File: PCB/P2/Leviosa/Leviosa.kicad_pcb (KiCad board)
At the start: 2 copper layers, 80 x 80 mm, 51 parts, among them J1 Barrel_Jack, J2 2.54mm 1x03 Spare

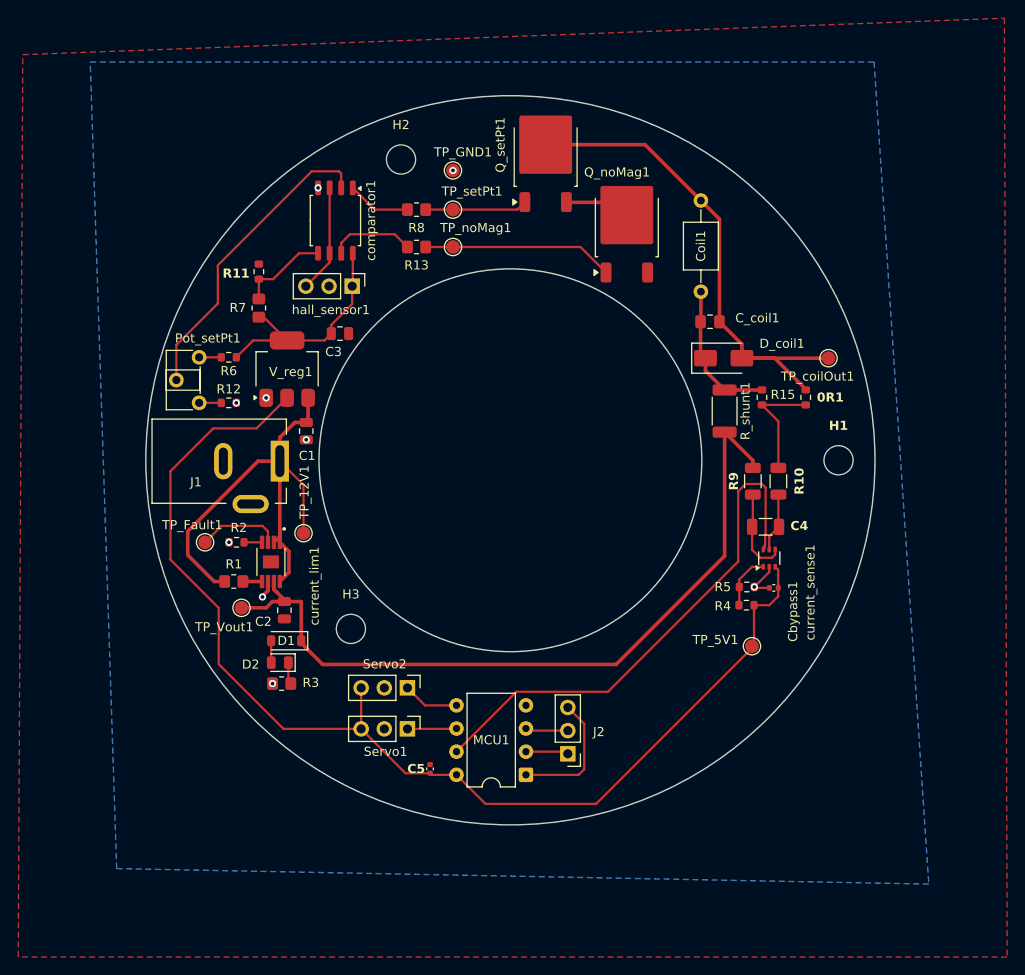
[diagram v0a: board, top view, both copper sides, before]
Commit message: update schematic and pcb per Jack's feedback
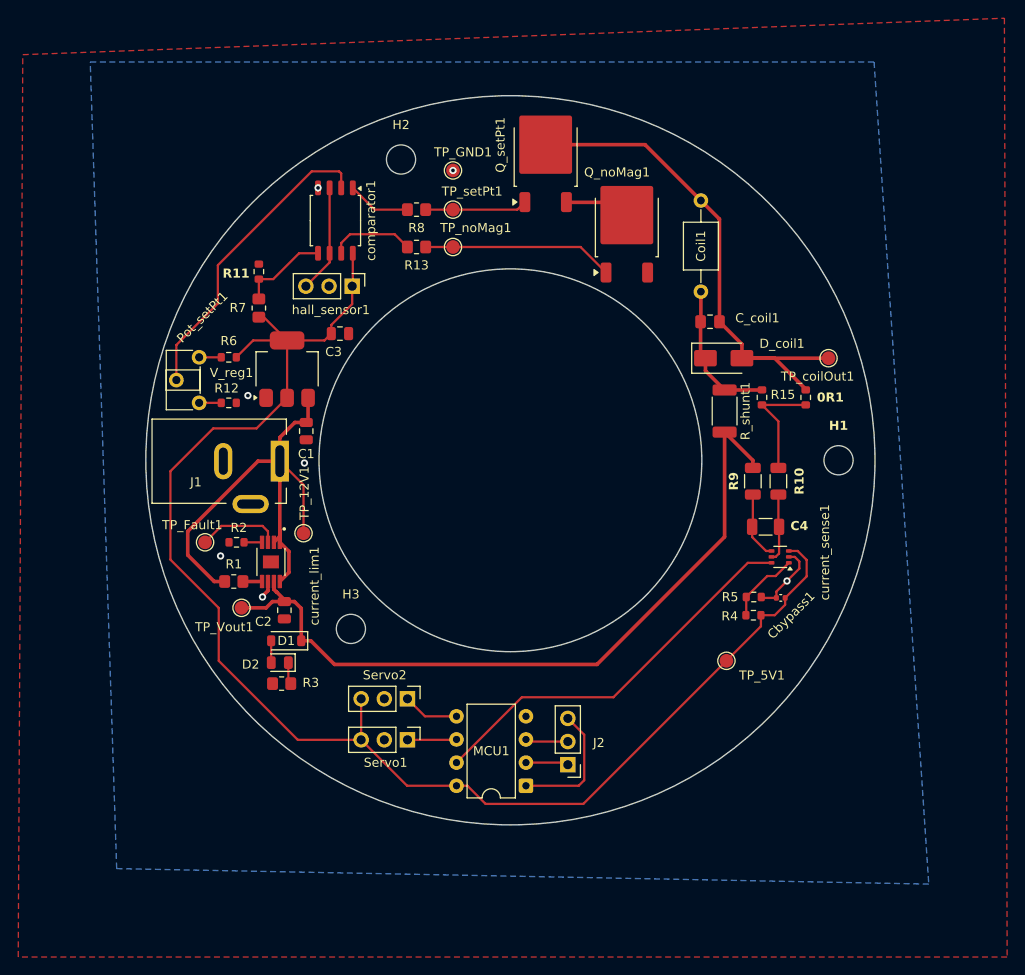
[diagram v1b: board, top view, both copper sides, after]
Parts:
- removed C5: 0.1µF, Capacitor_SMD:C_0402_1005Metric
- R10: value 8.2Ω -> 8Ω
- moved TP_5V1 3.22 mm to (123.7, 122.0)
- moved R5 1.34 mm to (126.7, 115.0)
- moved Cbypass1 1.34 mm to (129.7, 115.1)
- moved R4 1.34 mm to (126.7, 117.0)
- moved current_sense1 1.21 mm to (129.6, 110.6), turned to 180 degrees
- moved J2 1.20 mm to (106.3, 133.4)
- moved MCU1 1.20 mm to (101.7, 135.7)
- moved Servo2 1.20 mm to (88.7, 126.2)
- moved Servo1 1.20 mm to (88.7, 130.7)
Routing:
- net /current_sense: track 57.6 -> 43.6 mm
- net /5V: track 152.6 -> 162.0 mm
- net GND: track 6.54 -> 9.91 mm, vias 9 -> 7
- net Net-(current_sense1-+): track 9.69 -> 7.45 mm
- net Net-(current_sense1-REF): track 6.05 -> 8.19 mm
- net /V_out: track 85.3 -> 83.5 mm
- net Net-(current_sense1--): track 6.50 -> 7.47 mm

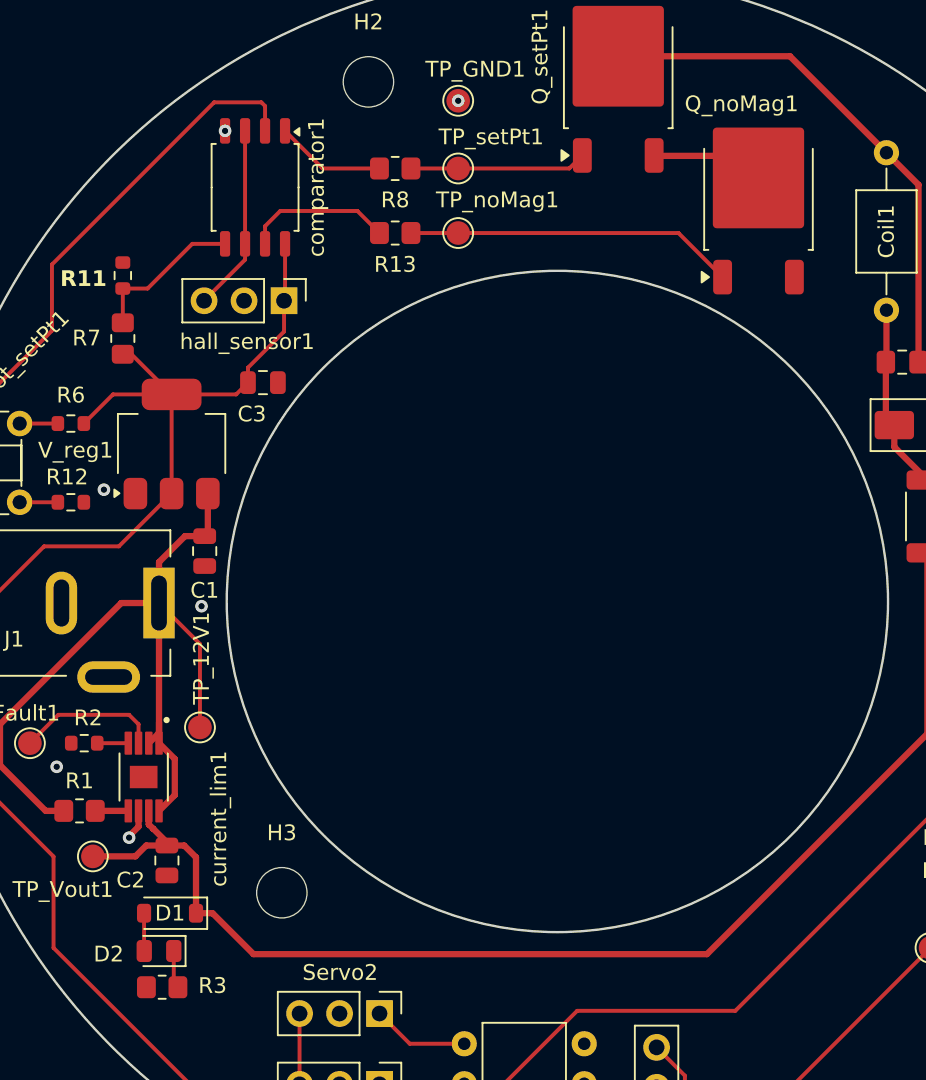
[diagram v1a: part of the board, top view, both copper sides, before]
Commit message: update PCB
pending trace width update potentially (long 5V and 12Vout)
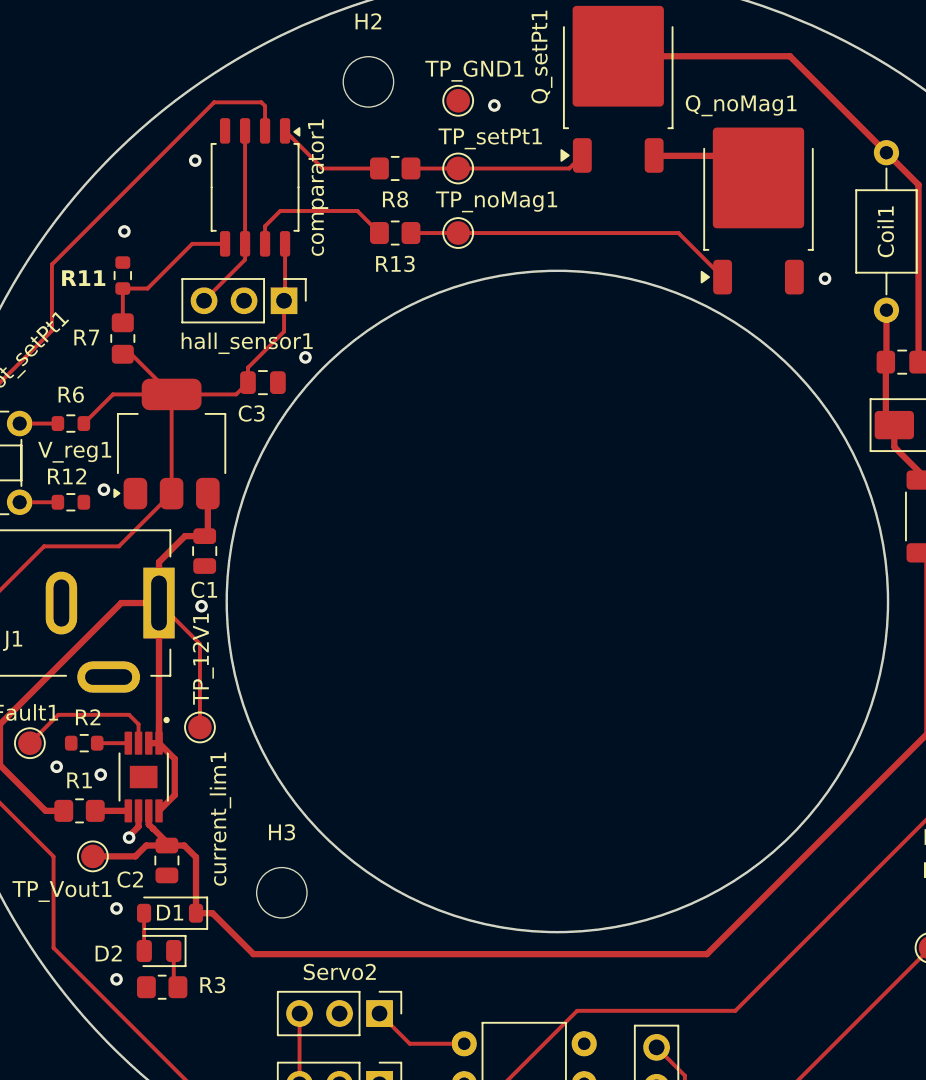
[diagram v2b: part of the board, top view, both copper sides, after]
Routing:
- net GND: vias 7 -> 13
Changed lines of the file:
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@@
+	)
+	(segment
+		(start 74.05 109)
+		(end 74.7 109)
+		(width 0.4)
+		(layer "F.Cu")
+		(net 1)
 	)
 	(segment
@@
 	)
 	(segment
-		(start 74.05 109)
-		(end 74.7 108.35)
-		(width 0.4)
-		(layer "F.Cu")
-		(net 1)
-	)
-	(segment
 		(start 77.8 93.15)
 		(end 77.8 95.65)
@@
 	)
 	(via
-		(at 78.895 70.1125)
+		(at 77 72)
+		(size 0.8)
+		(drill 0.4)
+		(layers "F.Cu" "B.Cu")
+		(net 3)
+	)
+	(via
+		(at 72.5 76.5)
 		(size 0.8)
 		(drill 0.4)
@@
 	)
 	(via
+		(at 84 84.5)
+		(size 0.8)
+		(drill 0.4)
+		(layers "F.Cu" "B.Cu")
+		(net 3)
+	)
+	(via
 		(at 130.343126 113.243126)
 		(size 0.8)
@@
 	)
 	(via
+		(at 117 79.5)
+		(size 0.8)
+		(drill 0.4)
+		(layers "F.Cu" "B.Cu")
+		(net 3)
+	)
+	(via
+		(at 72 124)
+		(size 0.8)
+		(drill 0.4)
+		(layers "F.Cu" "B.Cu")
+		(net 3)
+	)
+	(via
+		(at 72 119.5)
+		(size 0.8)
+		(drill 0.4)
+		(layers "F.Cu" "B.Cu")
+		(net 3)
+	)
+	(via
 		(at 68.2 110.5)
 		(size 0.8)
@@
 	)
 	(via
-		(at 93.7 68.2)
+		(at 96 68.5)
 		(size 0.8)
 		(drill 0.4)
@@
 		(net 3)
 	)
+	(via
+		(at 71 111)
+		(size 0.8)
+		(drill 0.4)
+		(layers "F.Cu" "B.Cu")
+		(net 3)
+	)

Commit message: update pcb
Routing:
- added copper zone on F.Cu, net +12V
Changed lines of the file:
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@@
 		(tags "LED")
 		(property "Reference" "D2"
-			(at 3.2 -0.2 0)
+			(at 3.2 0.3 0)
 			(unlocked yes)
 			(layer "F.SilkS")
@@
 	)
 	(segment
+		(start 75.5 94.15)
+		(end 73.45 96.2)
+		(width 0.8)
+		(layer "F.Cu")
+		(net 2)
+	)
+	(segment
 		(start 94.085 135.71)
 		(end 95.285 135.71)
@@
 	(segment
 		(start 75.5 93.15)
-		(end 75.5 86.85)
-		(width 0.25)
+		(end 75.5 94.15)
+		(width 0.8)
 		(layer "F.Cu")
 		(net 2)
@@
 	)
 	(segment
-		(start 72.15 96.5)
-		(end 67.4 96.5)
-		(width 0.25)
+		(start 73.45 96.2)
+		(end 67 96.2)
+		(width 0.8)
 		(layer "F.Cu")
 		(net 2)
@@
 	)
 	(segment
-		(start 76.67 130.67)
-		(end 83.625 130.67)
-		(width 0.25)
-		(layer "F.Cu")
-		(net 2)
-	)
-	(segment
 		(start 79.6 86.85)
 		(end 75.5 86.85)
@@
 	)
 	(segment
-		(start 62.7 110.9)
-		(end 68 116.2)
-		(width 0.25)
+		(start 62.9 111.2)
+		(end 68.1 116.4)
+		(width 0.8)
 		(layer "F.Cu")
 		(net 2)
@@
 	)
 	(segment
-		(start 67.4 96.5)
-		(end 62.7 101.2)
-		(width 0.25)
+		(start 77.254372 130.67)
+		(end 83.625 130.67)
+		(width 0.8)
 		(layer "F.Cu")
 		(net 2)
@@
 	)
 	(segment
-		(start 62.7 101.2)
-		(end 62.7 110.9)
+		(start 82.64 82.86)
+		(end 80.35 85.15)
 		(width 0.25)
 		(layer "F.Cu")
@@
 	)
 	(segment
-		(start 68 122)
-		(end 76.67 130.67)
-		(width 0.25)
+		(start 68.1 121.515628)
+		(end 77.254372 130.67)
+		(width 0.8)
 		(layer "F.Cu")
 		(net 2)
 	)
 	(segment
-		(start 82.64 82.86)
-		(end 80.35 85.15)
+		(start 83.625 126.17)
+		(end 83.625 130.67)
 		(width 0.25)
 		(layer "F.Cu")
@@
 	)
 	(segment
-		(start 75.5 93.15)
-		(end 72.15 96.5)
+		(start 88.665 135.71)
+		(end 83.625 130.67)
 		(width 0.25)
 		(layer "F.Cu")
@@
 	)
 	(segment
-		(start 68 116.2)
-		(end 68 122)
-		(width 0.25)
+		(start 75.5 93.15)
+		(end 75.5 86.85)
+		(width 0.8)
 		(layer "F.Cu")
 		(net 2)
 	)
 	(segment
-		(start 83.625 126.17)
-		(end 83.625 130.67)
-		(width 0.25)
+		(start 67 96.2)
+		(end 62.9 100.3)
+		(width 0.8)
 		(layer "F.Cu")
 		(net 2)
 	)
 	(segment
-		(start 88.665 135.71)
-		(end 83.625 130.67)
+		(start 71.775 86.85)
+		(end 69.925 88.7)
 		(width 0.25)
 		(layer "F.Cu")
@@
 	)
 	(segment
-		(start 71.775 86.85)
-		(end 69.925 88.7)
-		(width 0.25)
+		(start 62.9 100.3)
+		(end 62.9 111.2)
+		(width 0.8)
 		(layer "F.Cu")
 		(net 2)
@@
 	)
 	(segment
+		(start 68.1 116.4)
+		(end 68.1 121.515628)
+		(width 0.8)
+		(layer "F.Cu")
+		(net 2)
+	)
+	(segment
 		(start 80.35 86.1)
 		(end 79.6 86.85)
@@
 	)
 	(via
-		(at 77 72)
+		(at 77 71.8)
 		(size 0.8)
 		(drill 0.4)
@@
 	)
 	(via
-		(at 72.5 76.5)
+		(at 72.4 76.7)
 		(size 0.8)
 		(drill 0.4)
@@
 	)
 	(via
-		(at 72 124)
+		(at 72.2 123.3)
 		(size 0.8)
 		(drill 0.4)
@@
 	)
 	(via
-		(at 96 68.5)
+		(at 95.9 68.2)
 		(size 0.8)
 		(drill 0.4)
@@
 	)
 	(zone
+		(net 1)
+		(net_name "+12V")
+		(layer "F.Cu")
+		(hatch edge 0.5)
+		(priority 2)
+		(connect_pads
+			(clearance 0.5)
+		)
+		(min_thickness 0.25)
+		(filled_areas_thickness no)
+		(fill
+			(thermal_gap 0.5)
+			(thermal_bridge_width 0.5)
+		)
+		(polygon
+			(pts
+				(xy 73.87 108.3) (xy 74.5 108.3) (xy 74.5 102.3) (xy 75.7 101.6) (xy 78.4 103.8) (xy 78.4 112.1)
+				(xy 74.9 114) (xy 74.5 114) (xy 74.5 112.6) (xy 74.9 112.6) (xy 75.6 111.9) (xy 75.6 110.4) (xy 74.9 109.7)
+				(xy 73.87 109.7)
+			)
+		)
+	)
+	(zone

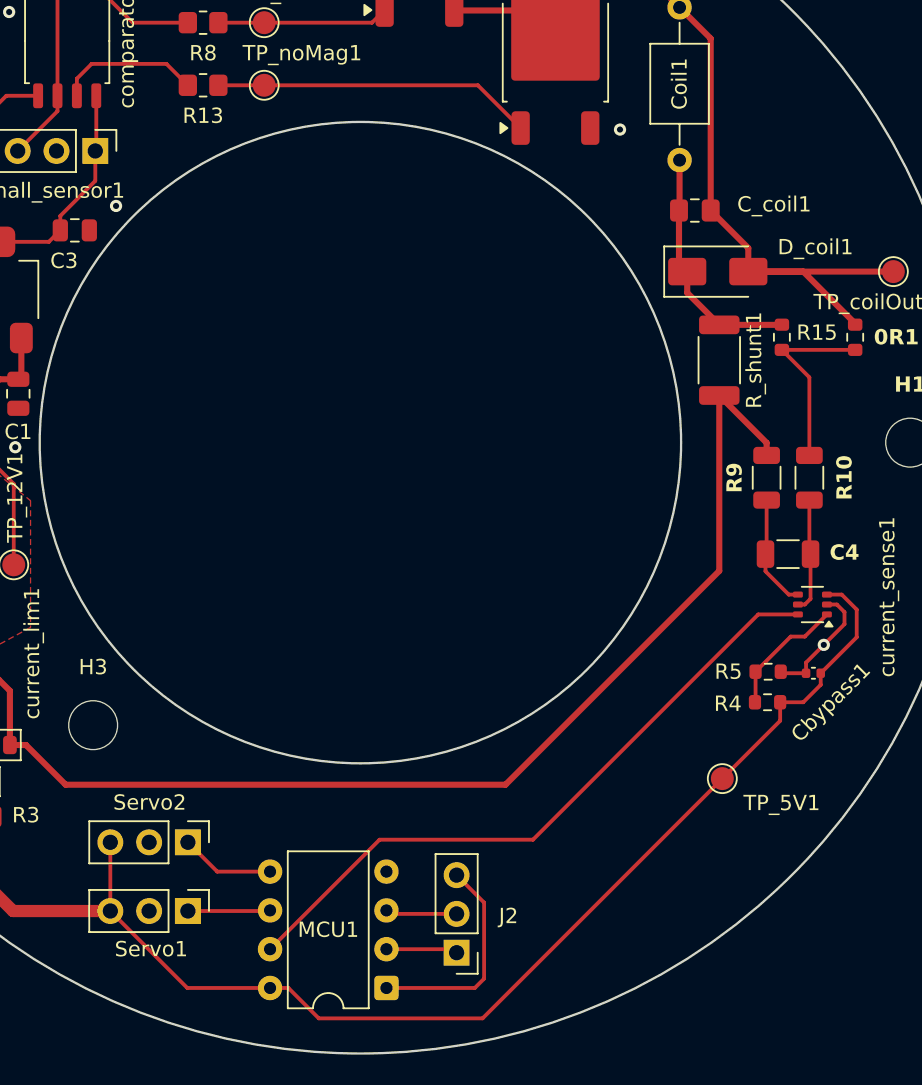
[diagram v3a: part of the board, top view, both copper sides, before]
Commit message: add fiducials and add thickness to 5V
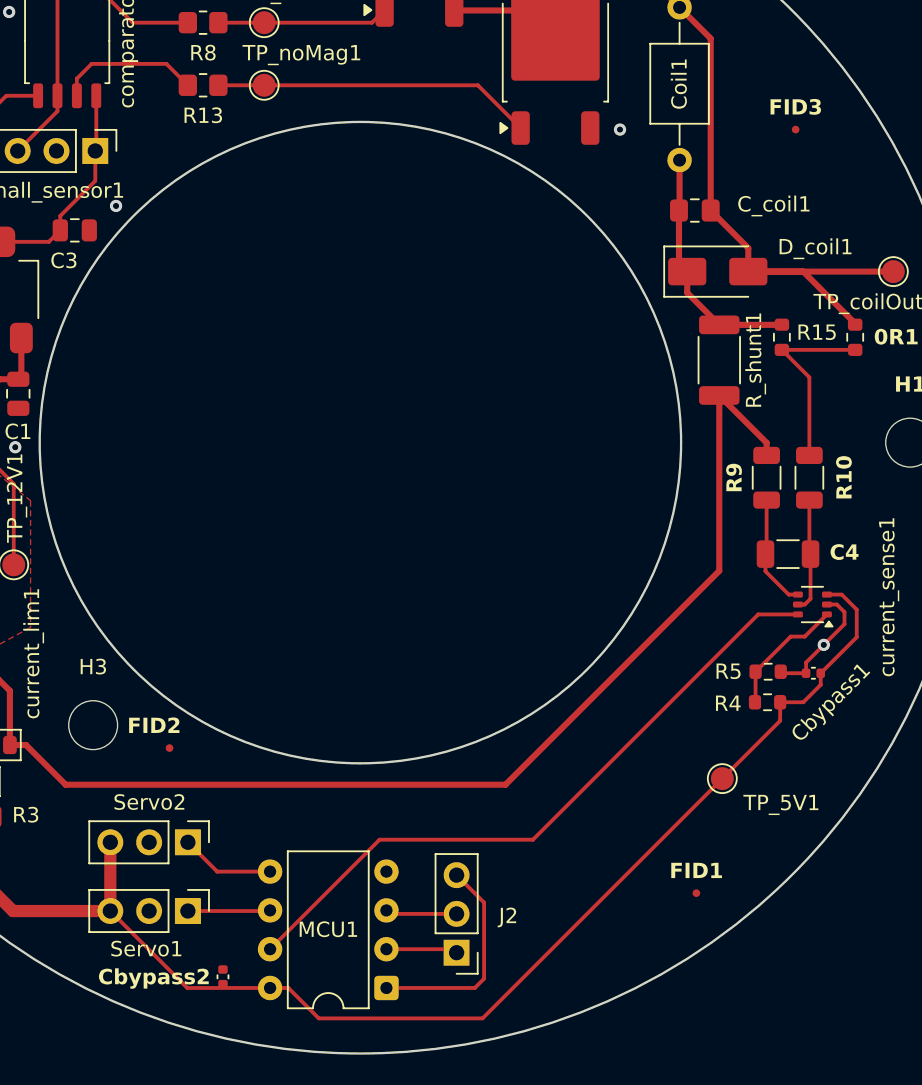
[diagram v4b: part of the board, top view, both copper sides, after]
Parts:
- added Cbypass2: 0.1µF, Capacitor_SMD:C_0402_1005Metric, F.Cu at (91.0, 135.0)
- added FID1: Fiducial, Fiducial:Fiducial_0.5mm_Mask1mm, F.Cu at (122.0, 129.5)
- added FID2: Fiducial, Fiducial:Fiducial_0.5mm_Mask1mm, F.Cu at (87.5, 120.0)
- added FID3: Fiducial, Fiducial:Fiducial_0.5mm_Mask1mm, F.Cu at (128.5, 79.5)
- R10: value 8Ω -> 8.2Ω
